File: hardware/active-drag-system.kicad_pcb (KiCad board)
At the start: 4 copper layers, 33 x 90 mm, 102 parts, among them J1 Conn_01x02_Pin, J2 Conn_01x02_Socket, J3 10118193-0001LF, J4 Conn_01x05_Pin, J5 Conn_01x02_Pin, J6 Conn_01x02_Pin, J7 Conn_01x03_Pin, J8 Conn_01x03_Pin, SW1 PTS815 SJM 250 SMTR LFS, U1 RP2040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

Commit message: Rev 2
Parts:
- added TP10: nSLEEP, TestPoint:TestPoint_Pad_1.0x1.0mm, F.Cu at (157.9, 137.4)
- added TP11: DRVOFF, TestPoint:TestPoint_Pad_1.0x1.0mm, F.Cu at (153.3, 140.8)
- added TP12: BRAKE, TestPoint:TestPoint_Pad_1.0x1.0mm, B.Cu at (144.6, 125.9)
- added TP13: SPI_TX, TestPoint:TestPoint_Pad_1.0x1.0mm, F.Cu at (154.8, 128.0)
- added TP14: SPI_CSn, TestPoint:TestPoint_Pad_1.0x1.0mm, B.Cu at (147.6, 130.7)
- added TP15: SPI_SCK, TestPoint:TestPoint_Pad_1.0x1.0mm, F.Cu at (152.5, 130.2)
- added TP16: SPI_RX, TestPoint:TestPoint_Pad_1.0x1.0mm, F.Cu at (157.2, 128.0)
- added TP17: CLKIN, TestPoint:TestPoint_Pad_1.0x1.0mm, F.Cu at (155.0, 86.2)
- added TP18: MGINT, TestPoint:TestPoint_Pad_1.0x1.0mm, B.Cu at (159.2, 84.5)
- added TP19: MINT, TestPoint:TestPoint_Pad_1.0x1.0mm, B.Cu at (161.3, 71.5)
- added TP20: HGINT1, TestPoint:TestPoint_Pad_1.0x1.0mm, B.Cu at (157.4, 91.2)
- added TP21: HGINT2, TestPoint:TestPoint_Pad_1.0x1.0mm, F.Cu at (155.8, 95.8)
- added TP22: FGOUT, TestPoint:TestPoint_Pad_1.0x1.0mm, B.Cu at (133.5, 118.2)
- added TP9: nFAULT, TestPoint:TestPoint_Pad_1.0x1.0mm, F.Cu at (157.2, 140.8)
- J6: value Conn_01x02_Pin -> Conn_01x04_Pin; footprint Connector_PinHeader_2.54mm:PinHeader_1x02_P2.54mm_Vertical -> Connector_PinHeader_2.54mm:PinHeader_1x04_P2.54mm_Vertical
- moved J6 5.07 mm to (133.6, 113.6)
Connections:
- J6 pad 1: /MCU_RP2040/I2C1_SCL -> /+3V3
- J6 pad 2: /MCU_RP2040/I2C1_SDA -> GND
- U1 pad 7: unconnected-(U1-GPIO5-Pad7) -> /MCU_RP2040/FGOUT
- U1 pad 8: /MCU_RP2040/FGOUT -> unconnected-(U1-GPIO6-Pad8)
- U7 pad 11: GND -> unconnected-(U7-RESERVED-Pad11)
- U7 pad 3: GND -> unconnected-(U7-RESERVED-Pad3)
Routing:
- net /MCU_RP2040/SPI0_TX: track 54.7 -> 66.5 mm
- net /MAG: track 23.7 -> 30.7 mm, vias 2 -> 3
- net /MCU_RP2040/nSLEEP: track 57.5 -> 64.5 mm
- net /MCU_RP2040/SPI0_RX: track 53.5 -> 60.4 mm
- net /MCU_RP2040/nFAULT: track 59.6 -> 64.5 mm
- net /MCU_RP2040/SPI0_SCK: track 55.8 -> 60.0 mm
- net /MCU_RP2040/FGOUT: track 60.1 -> 62.1 mm
- net /HG2: track 10.3 -> 12.2 mm
- net /HG1: track 9.52 -> 11.3 mm, vias 0 -> 1
- net /MCU_RP2040/BRAKE: track 53.7 -> 55.5 mm
- net /MCU_RP2040/DRVOFF: track 60.0 -> 61.6 mm
- net /MG: track 12.6 -> 13.9 mm
- net /MCU_RP2040/CLKOUT: track 7.63 -> 8.66 mm
- net GND: track 236.4 -> 237.4 mm, vias 73 -> 74
- net /+3V3: track 21.8 -> 22.2 mm, vias 10 -> 14
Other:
- board text added: "Active Drag System: Rev 2 Designed by: Dawsyn Schraiber Kemper Brown Cian Capacci with help from Gabe Mills"
- board text added: "SWDIO GND SWCLK"
- board text added: "TX RX SDA SCL GND 3v3"
- board text removed: "Active Drag System: Rev 1 Designed by: Dawsyn Schraiber Kemper Brown Cian Capacci with help from Gabe Mills"

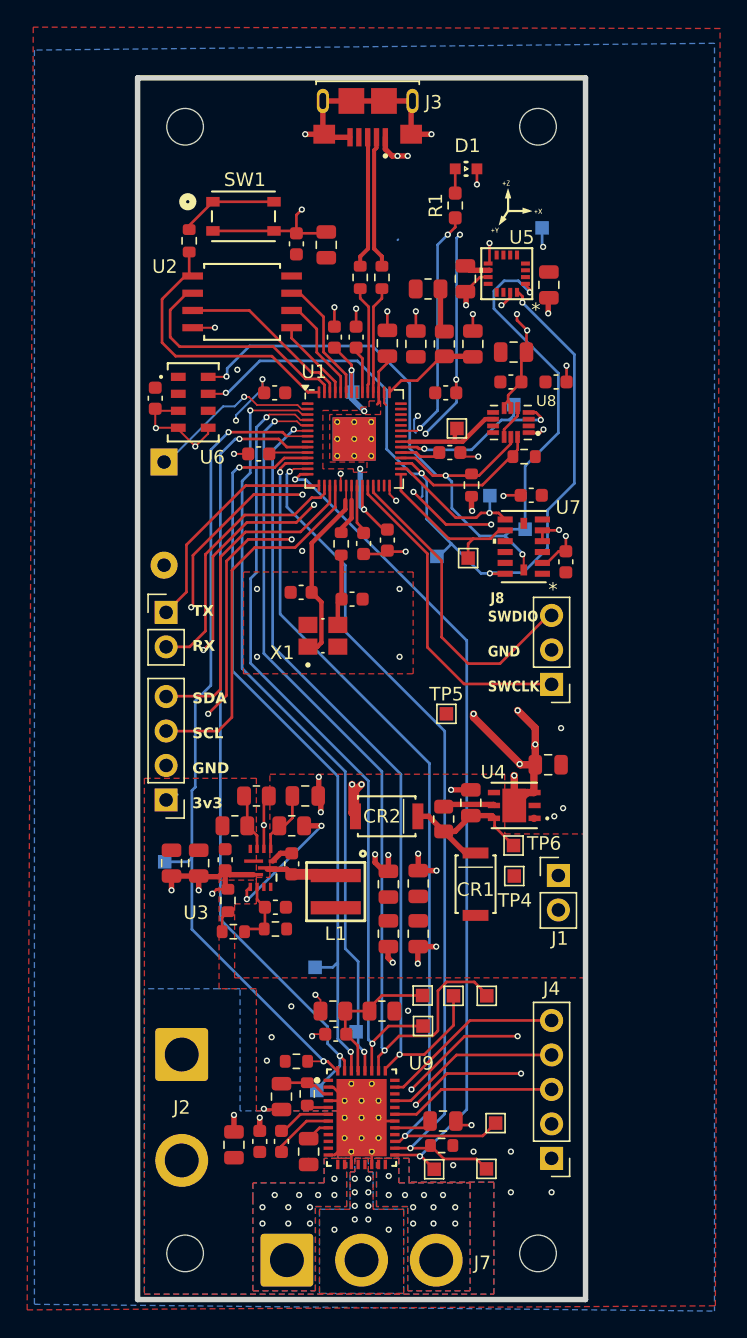
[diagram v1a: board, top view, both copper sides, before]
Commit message: version of pcb with no motor driver, only previously used servo enable and pwm circuit
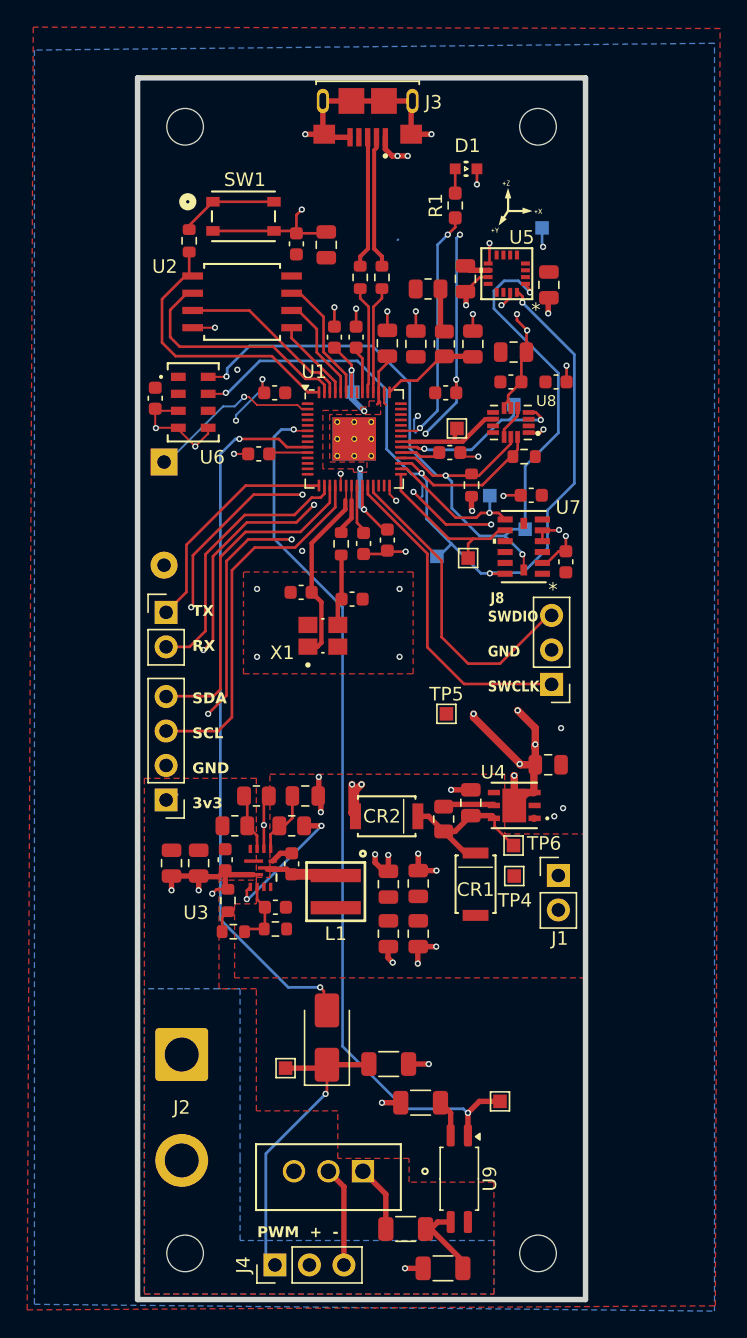
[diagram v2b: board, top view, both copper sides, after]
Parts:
- removed C36, C40: 100nF, Capacitor_SMD:C_0603_1608Metric
- removed C37: 10uF, Capacitor_SMD:C_0805_2012Metric
- removed C38: 47nF, Capacitor_SMD:C_0603_1608Metric
- removed C39, C41: 1uF, Capacitor_SMD:C_0805_2012Metric
- removed C42: 22uF, Capacitor_SMD:C_0805_2012Metric
- removed J7: Conn_01x03_Pin, active-drag-system:SolderWire-2sqmm_1x03_P7.8mm_D2mm_OD3.9mm
- removed R21: 10k, Resistor_SMD:R_0603_1608Metric
- removed TP10: nSLEEP, TestPoint:TestPoint_Pad_1.0x1.0mm
- removed TP11: DRVOFF, TestPoint:TestPoint_Pad_1.0x1.0mm
- removed TP12: BRAKE, TestPoint:TestPoint_Pad_1.0x1.0mm
- removed TP13: SPI_TX, TestPoint:TestPoint_Pad_1.0x1.0mm
- removed TP14: SPI_CSn, TestPoint:TestPoint_Pad_1.0x1.0mm
- removed TP15: SPI_SCK, TestPoint:TestPoint_Pad_1.0x1.0mm
- removed TP16: SPI_RX, TestPoint:TestPoint_Pad_1.0x1.0mm
- removed TP22: FGOUT, TestPoint:TestPoint_Pad_1.0x1.0mm
- removed TP9: nFAULT, TestPoint:TestPoint_Pad_1.0x1.0mm
- added D2: S1G, Diode_SMD:D_SMA, F.Cu at (145.4, 131.1)
- added U10: STP55NF06, active-drag-system:STP55NF06, F.Cu at (148.1, 140.9)
- J4: value Conn_01x05_Pin -> Conn_01x03_Pin; footprint Connector_PinHeader_2.54mm:PinHeader_1x05_P2.54mm_Vertical -> Connector_PinHeader_2.54mm:PinHeader_1x03_P2.54mm_Vertical
- R17: value 164k -> 4.7k; footprint Resistor_SMD:R_0805_2012Metric -> Resistor_SMD:R_1206_3216Metric
- R18: value 100k -> 4.7k; footprint Resistor_SMD:R_0805_2012Metric -> Resistor_SMD:R_1206_3216Metric
- R19: value 10k -> 1k; footprint Resistor_SMD:R_0603_1608Metric -> Resistor_SMD:R_1206_3216Metric
- R20: value 22 -> 220; footprint Resistor_SMD:R_0603_1608Metric -> Resistor_SMD:R_1206_3216Metric
- TP7: value ILIM -> SERVO_ENABLE
- TP8: value PWM -> SERVO_PWM; moved to F.Cu
- U9: value MCT8316Z0RRGFR -> FODM217A; footprint active-drag-system:RGF0040E-MFG -> Package_SO:SOP-4_4.4x2.6mm_P1.27mm
- moved J4 21.8 mm to (141.6, 147.8), turned to 90 degrees
- moved R18 20.6 mm to (154.0, 148.1)
- moved R19 14.7 mm to (151.2, 145.2)
- moved TP7 9.66 mm to (158.2, 135.8)
- moved U9 8.49 mm to (155.2, 141.5), turned to -90 degrees
- moved R20 8.38 mm to (152.3, 135.9), turned to 0 degrees
- moved R17 3.93 mm to (150.0, 133.1), turned to 180 degrees
- moved TP8 2.83 mm to (142.4, 133.3), turned to 0 degrees
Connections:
- J4 pad 1: /+3V3 -> Net-(D2-K)
- J4 pad 2: GND -> /VBAT
- J4 pad 3: /Motor Driver/HALL_SENSE_A -> Net-(J4-Pin_3)
- R17 pad 1: Net-(U9-ILIM) -> GND
- R17 pad 2: /+3V3 -> Net-(D2-K)
- R18 pad 1: Net-(U9-ILIM) -> Net-(R18-Pad1)
- R19 pad 1: /+3V3 -> Net-(R19-Pad1)
- R19 pad 2: /MCU_RP2040/FGOUT -> Net-(R18-Pad1)
- R20 pad 1: Net-(U9-SW_BK) -> GND
- R20 pad 2: Net-(U9-FB_BK) -> Net-(R20-Pad2)
- TP7 pad 1: Net-(U9-ILIM) -> /MCU_RP2040/SERVO_ENABLE
- TP8 pad 1: /MCU_RP2040/MOTOR_PWM -> Net-(D2-K)
- U1 pad 11: /MCU_RP2040/BRAKE -> unconnected-(U1-GPIO8-Pad11)
- U1 pad 12: /MCU_RP2040/nSLEEP -> unconnected-(U1-GPIO9-Pad12)
- U1 pad 13: /MCU_RP2040/nFAULT -> unconnected-(U1-GPIO10-Pad13)
- U1 pad 14: /MCU_RP2040/DRVOFF -> unconnected-(U1-GPIO11-Pad14)
- U1 pad 3: /MCU_RP2040/SPI0_CSn0 -> unconnected-(U1-GPIO1-Pad3)
- U1 pad 4: /MCU_RP2040/SPI0_SCK -> unconnected-(U1-GPIO2-Pad4)
- U1 pad 5: /MCU_RP2040/SPI0_TX -> unconnected-(U1-GPIO3-Pad5)
- U1 pad 6: /MCU_RP2040/SPI0_RX -> /MCU_RP2040/SERVO_ENABLE
- U1 pad 7: /MCU_RP2040/FGOUT -> unconnected-(U1-GPIO5-Pad7)
- U9 pad 1: unconnected-(U9-NC-Pad1) -> /MCU_RP2040/SERVO_ENABLE
- U9 pad 2: GND -> Net-(R20-Pad2)
- U9 pad 3: Net-(U9-FB_BK) -> Net-(R18-Pad1)
- U9 pad 4: GND -> /VBAT
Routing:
- net /MCU_RP2040/SPI0_TX: track 66.5 -> 0.00 mm, vias 2 -> 0
- net /MCU_RP2040/SERVO_ENABLE: track 0.00 -> 65.4 mm, vias 0 -> 2
- net /MCU_RP2040/nSLEEP: track 64.5 -> 0.00 mm, vias 2 -> 0
- net /MCU_RP2040/nFAULT: track 64.5 -> 0.00 mm, vias 2 -> 0
- net /MCU_RP2040/FGOUT: track 62.1 -> 0.00 mm, vias 2 -> 0
- net /MCU_RP2040/DRVOFF: track 61.6 -> 0.00 mm, vias 2 -> 0
- net /MCU_RP2040/SPI0_RX: track 60.4 -> 0.00 mm, vias 2 -> 0
- net /MCU_RP2040/SPI0_SCK: track 60.0 -> 0.00 mm, vias 2 -> 0
- net /MCU_RP2040/SPI0_CSn0: track 57.0 -> 0.00 mm, vias 2 -> 0
- net /MCU_RP2040/BRAKE: track 55.5 -> 0.00 mm, vias 2 -> 0
- net GND: track 237.4 -> 201.6 mm, vias 74 -> 67
- net Net-(D2-K): track 0.00 -> 23.2 mm, vias 0 -> 1
- net /Motor Driver/HALL_SENSE_C: track 13.6 -> 0.00 mm
- net /Motor Driver/HALL_SENSE_B: track 13.0 -> 0.00 mm
- net /Motor Driver/HALL_SENSE_A: track 12.4 -> 0.00 mm
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- removed copper zone on B.Cu, net /Motor Driver/PHASE_A
- removed copper zone on F.Cu, net /Motor Driver/PHASE_A
- removed copper zone on B.Cu, net /Motor Driver/PHASE_B
- removed copper zone on F.Cu, net /Motor Driver/PHASE_B
- removed copper zone on B.Cu, net /Motor Driver/PHASE_C
- removed copper zone on F.Cu, net /Motor Driver/PHASE_C
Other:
- board text added: "Active Drag System: Rev 2 (Backup) Designed by: Dawsyn Schraiber Kemper Brown Cian Capacci with help from Gabe Mills"
- board text added: "PWM + -"
- board text removed: "Active Drag System: Rev 2 Designed by: Dawsyn Schraiber Kemper Brown Cian Capacci with help from Gabe Mills"
